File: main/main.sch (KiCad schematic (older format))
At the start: 2 parts, among them J2 AudioJack3, J3 Conn_02x10_Odd_Even

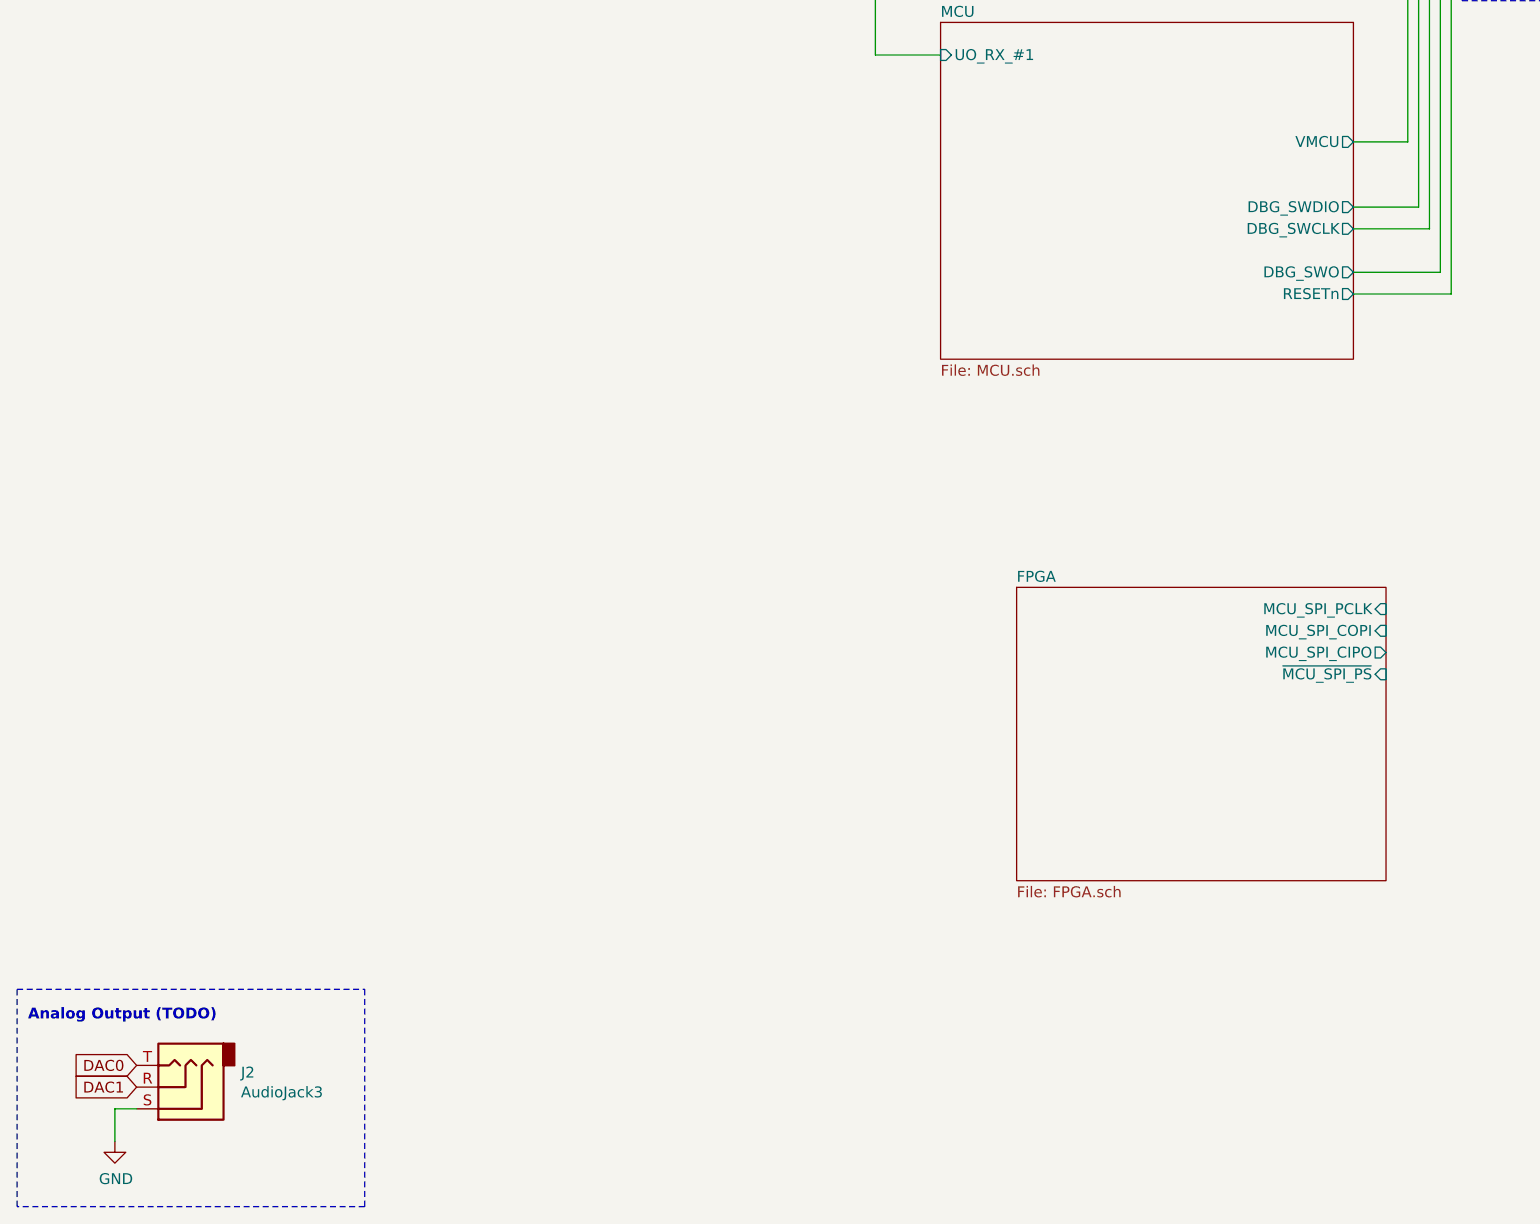
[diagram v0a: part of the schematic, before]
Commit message: Setup DAC.
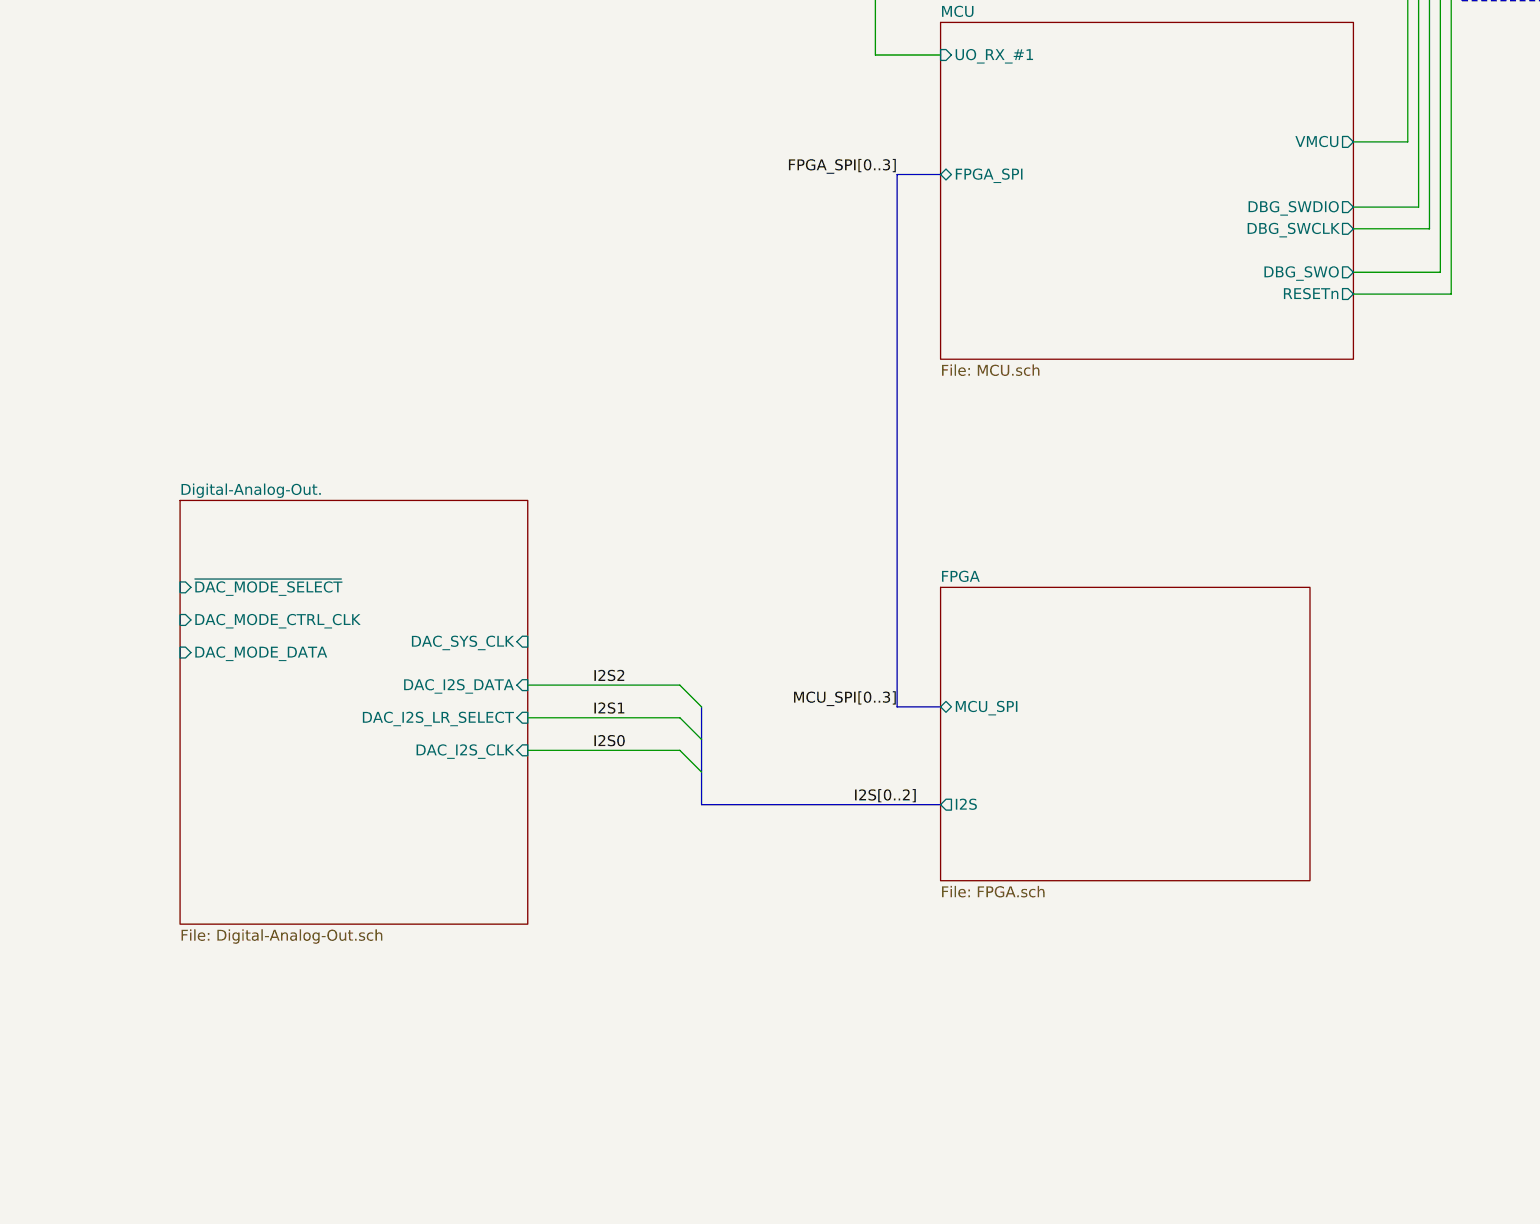
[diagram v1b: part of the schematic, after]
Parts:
- removed J2: AudioJack3, symbol Connector:AudioJack3
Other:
- note removed: "Analog Output (TODO)"
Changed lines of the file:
@@
 $Descr A4 11693 8268
 encoding utf-8
-Sheet 1 4
+Sheet 1 5
 Title "Synthesizer"
 Date "2021-09-06"
@@
 Comment4 "TDT4295 Computer Design Project"
 $EndDescr
-$Comp
-L Connector:AudioJack3 J2
-U 1 1 61366BDF
-P 1300 7150
-F 0 "J2" H 1020 7083 50  0000 R CNN
-F 1 "AudioJack3" H 1020 7174 50  0000 R CNN
-F 2 "" H 1300 7150 50  0001 C CNN
-F 3 "~" H 1300 7150 50  0001 C CNN
-	1    1300 7150
-	-1   0    0    1
-$EndComp
-$Comp
-L power:GND #PWR0101
-U 1 1 61367C82
-P 1000 7400
-F 0 "#PWR0101" H 1000 7150 50  0001 C CNN
-F 1 "GND" H 1005 7227 50  0000 C CNN
-F 2 "" H 1000 7400 50  0001 C CNN
-F 3 "" H 1000 7400 50  0001 C CNN
-	1    1000 7400
-	1    0    0    -1
-$EndComp
-Wire Wire Line
-	1000 7400 1000 7250
-Wire Wire Line
-	1000 7250 1100 7250
-Text GLabel 1100 7050 0    50   Input ~ 0
-DAC0
-Text GLabel 1100 7150 0    50   Input ~ 0
-DAC1
-Wire Notes Line
-	550  6700 2150 6700
-Wire Notes Line
-	2150 7700 550  7700
-Text Notes 600  6850 0    50   ~ 10
-Analog Output (TODO)
-Wire Notes Line
-	2150 6700 2150 7700
-Wire Notes Line
-	550  7700 550  6700
 Wire Notes Line
 	11150 550  7200 550
-$Sheet
-S 4800 2250 1900 1550
-U 6139E7E0
-F0 "MCU" 50
-F1 "MCU.sch" 50
-F2 "DBG_SWDIO" O R 6700 3100 50
-F3 "DBG_SWCLK" O R 6700 3200 50
-F4 "DBG_SWO" O R 6700 3400 50
-F5 "RESETn" O R 6700 3500 50
-F6 "VMCU" O R 6700 2800 50
-F7 "UO_RX_#1" I L 4800 2400 50
-$EndSheet
 $Sheet
 S 3450 700  700  250
@@
 	4500 2400 4800 2400
 $Sheet
-S 5150 4850 1700 1350
+S 1300 4450 1600 1950
+U 61417224
+F0 "Digital-Analog-Out." 50
+F1 "Digital-Analog-Out.sch" 50
+F2 "~DAC_MODE_SELECT" I L 1300 4850 50
+F3 "DAC_MODE_CTRL_CLK" I L 1300 5000 50
+F4 "DAC_MODE_DATA" I L 1300 5150 50
+F5 "DAC_SYS_CLK" I R 2900 5100 50
+F6 "DAC_I2S_DATA" I R 2900 5300 50
+F7 "DAC_I2S_CLK" I R 2900 5600 50
+F8 "DAC_I2S_LR_SELECT" I R 2900 5450 50
+$EndSheet
+Entry Wire Line
+	3600 5300 3700 5400
+Entry Wire Line
+	3600 5450 3700 5550
+Entry Wire Line
+	3600 5600 3700 5700
+Wire Wire Line
+	2900 5300 3600 5300
+Wire Wire Line
+	2900 5450 3600 5450
+Wire Wire Line
+	2900 5600 3600 5600
+Text Label 4400 5850 0    50   ~ 0
+I2S[0..2]
+Text Label 3200 5300 0    50   ~ 0
+I2S2
+Text Label 3200 5450 0    50   ~ 0
+I2S1
+Text Label 3200 5600 0    50   ~ 0
+I2S0
+Wire Bus Line
+	3700 5850 4800 5850
+$Sheet
+S 4800 2250 1900 1550
+U 6139E7E0
+F0 "MCU" 50
+F1 "MCU.sch" 50
+F2 "DBG_SWDIO" O R 6700 3100 50
+F3 "DBG_SWCLK" O R 6700 3200 50
+F4 "DBG_SWO" O R 6700 3400 50
+F5 "RESETn" O R 6700 3500 50
+F6 "VMCU" O R 6700 2800 50
+F7 "UO_RX_#1" I L 4800 2400 50
+F8 "FPGA_SPI" B L 4800 2950 50
+$EndSheet
+$Sheet
+S 4800 4850 1700 1350
 U 613F0EEF
 F0 "FPGA" 50
 F1 "FPGA.sch" 50
-F2 "MCU_SPI_PCLK" I R 6850 4950 50
-F3 "MCU_SPI_COPI" I R 6850 5050 50
-F4 "MCU_SPI_CIPO" O R 6850 5150 50
-F5 "~MCU_SPI_PS" I R 6850 5250 50
-$EndSheet
+F2 "I2S" O L 4800 5850 50
+F3 "MCU_SPI" B L 4800 5400 50
+$EndSheet
+Wire Bus Line
+	4800 2950 4600 2950
+Wire Bus Line
+	4600 2950 4600 5400
+Wire Bus Line
+	4600 5400 4800 5400
+Text Label 4600 5400 2    50   ~ 0
+MCU_SPI[0..3]
+Text Label 4600 2950 2    50   ~ 0
+FPGA_SPI[0..3]
+Wire Bus Line
+	3700 5400 3700 5850
 $EndSCHEMATC

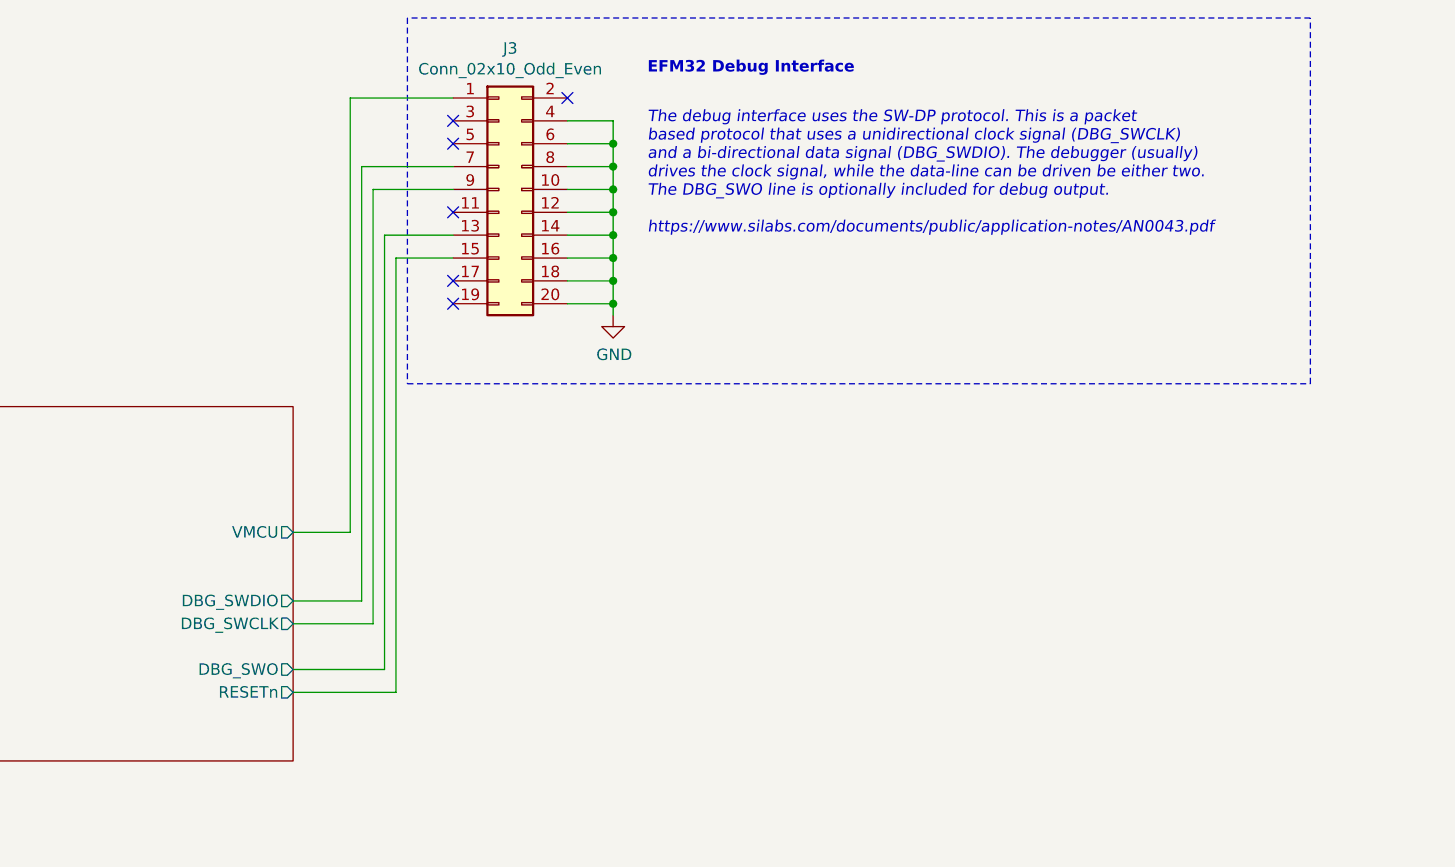
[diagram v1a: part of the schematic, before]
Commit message: Move EFM32GG debug port inside MCU sheet
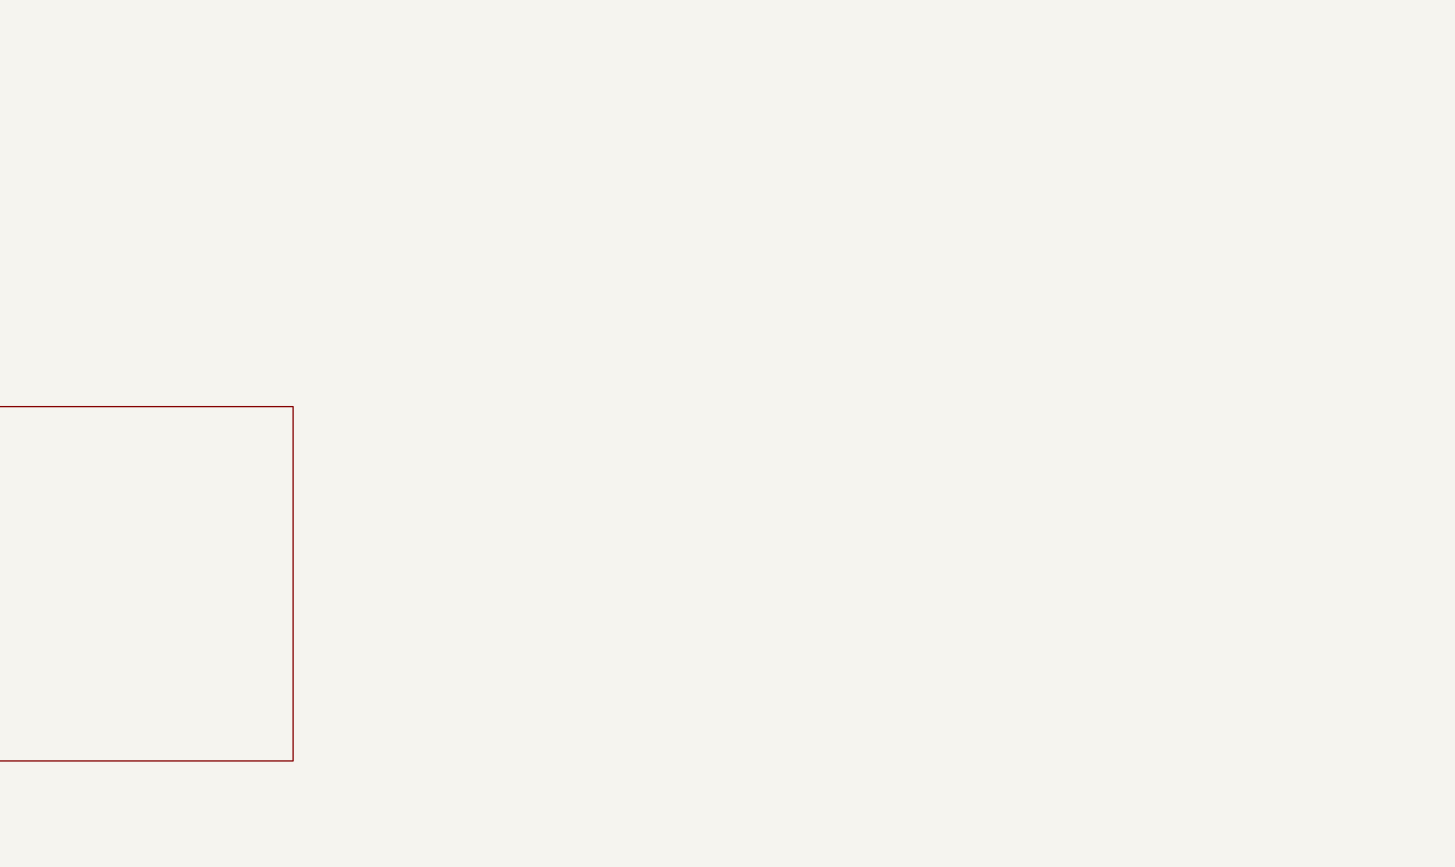
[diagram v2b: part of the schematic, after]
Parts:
- removed J3: Conn_02x10_Odd_Even, symbol Connector_Generic:Conn_02x10_Odd_Even
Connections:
- no-connect marks 6 -> 0
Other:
- note removed: "EFM32 Debug Interface"
- note removed: "The debug interface uses the SW-DP protocol. This is a packet \nbased protocol that uses a unidirectional clock signal (DBG_SWCLK) \nand a bi-directional data signal (DBG_SWDIO). The debugger (usually)\ndrives the clock signal, while the data-line can be driven be either two.\nThe DBG_SWO line is optionally included for debug output.\n\nhttps://www.silabs.com/documents/public/application-notes/AN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"
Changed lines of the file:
@@
 Comment4 "TDT4295 Computer Design Project"
 $EndDescr
-Wire Notes Line
-	11150 550  7200 550
 $Sheet
 S 3450 700  700  250
@@
 F2 "MIDI_IN" O R 4150 850 50
 $EndSheet
-Text Notes 8250 1500 0    50   Italic 0
-The debug interface uses the SW-DP protocol. This is a packet \nbased protocol that uses a unidirectional clock signal (DBG_SWCLK) \nand a bi-directional data signal (DBG_SWDIO). The debugger (usually)\ndrives the clock signal, while the data-line can be driven be either two.\nThe DBG_SWO line is optionally included for debug output.\n\nhttps://www.silabs.com/documents/public/application-notes/AN0043.pdf
-NoConn ~ 7400 1800
-NoConn ~ 7400 1700
-Wire Wire Line
-	8100 1100 8100 1200
-Connection ~ 8100 1100
-Wire Wire Line
-	8100 1000 8100 1100
-Wire Wire Line
-	7900 1000 8100 1000
-Connection ~ 8100 1200
-Wire Wire Line
-	7900 1100 8100 1100
-Wire Wire Line
-	8100 1300 8100 1400
-Connection ~ 8100 1300
-Wire Wire Line
-	8100 1200 8100 1300
-Wire Wire Line
-	7900 1200 8100 1200
-Connection ~ 8100 1400
-Wire Wire Line
-	7900 1300 8100 1300
-Wire Wire Line
-	8100 1500 8100 1600
-Connection ~ 8100 1500
-Wire Wire Line
-	8100 1400 8100 1500
-Wire Wire Line
-	7900 1400 8100 1400
-Wire Wire Line
-	8100 1600 8100 1700
-Connection ~ 8100 1600
-Wire Wire Line
-	7900 1500 8100 1500
-Connection ~ 8100 1700
-Wire Wire Line
-	7900 1600 8100 1600
-Wire Wire Line
-	8100 1800 8100 1850
-Connection ~ 8100 1800
-Wire Wire Line
-	8100 1700 8100 1800
-Wire Wire Line
-	7900 1700 8100 1700
-Wire Wire Line
-	7900 1800 8100 1800
-$Comp
-L power:GND #PWR04
-U 1 1 613B8CA5
-P 8100 1850
-F 0 "#PWR04" H 8100 1600 50  0001 C CNN
-F 1 "GND" H 8105 1677 50  0000 C CNN
-F 2 "" H 8100 1850 50  0001 C CNN
-F 3 "" H 8100 1850 50  0001 C CNN
-	1    8100 1850
-	1    0    0    -1
-$EndComp
-NoConn ~ 7400 1400
-NoConn ~ 7400 1100
-NoConn ~ 7400 1000
-NoConn ~ 7900 900
-$Comp
-L Connector_Generic:Conn_02x10_Odd_Even J3
-U 1 1 613A6A76
-P 7600 1300
-F 0 "J3" H 7650 1917 50  0000 C CNN
-F 1 "Conn_02x10_Odd_Even" H 7650 1826 50  0000 C CNN
-F 2 "" H 7600 1300 50  0001 C CNN
-F 3 "~" H 7600 1300 50  0001 C CNN
-	1    7600 1300
-	1    0    0    -1
-$EndComp
-Text Notes 8250 800  0    50   ~ 10
-EFM32 Debug Interface
-Wire Notes Line
-	7200 550  7200 2150
-Wire Notes Line
-	11150 2150 11150 550
-Wire Notes Line
-	7200 2150 11150 2150
-Wire Wire Line
-	6700 2800 6950 2800
-Wire Wire Line
-	6950 2800 6950 900
-Wire Wire Line
-	6950 900  7400 900
-Wire Wire Line
-	6700 3100 7000 3100
-Wire Wire Line
-	7000 3100 7000 1200
-Wire Wire Line
-	7000 1200 7400 1200
-Wire Wire Line
-	6700 3200 7050 3200
-Wire Wire Line
-	7050 3200 7050 1300
-Wire Wire Line
-	7050 1300 7400 1300
-Wire Wire Line
-	6700 3400 7100 3400
-Wire Wire Line
-	7100 3400 7100 1500
-Wire Wire Line
-	7100 1500 7400 1500
-Wire Wire Line
-	6700 3500 7150 3500
-Wire Wire Line
-	7150 3500 7150 1600
-Wire Wire Line
-	7150 1600 7400 1600
 Wire Wire Line
 	4150 850  4500 850
@@
 	3700 5850 4800 5850
 $Sheet
-S 4800 2250 1900 1550
-U 6139E7E0
-F0 "MCU" 50
-F1 "MCU.sch" 50
-F2 "DBG_SWDIO" O R 6700 3100 50
-F3 "DBG_SWCLK" O R 6700 3200 50
-F4 "DBG_SWO" O R 6700 3400 50
-F5 "RESETn" O R 6700 3500 50
-F6 "VMCU" O R 6700 2800 50
-F7 "UO_RX_#1" I L 4800 2400 50
-F8 "FPGA_SPI" B L 4800 2950 50
-$EndSheet
-$Sheet
 S 4800 4850 1700 1350
 U 613F0EEF
@@
 Text Label 4600 2950 2    50   ~ 0
 FPGA_SPI[0..3]
+$Sheet
+S 4800 2250 1900 1550
+U 6139E7E0
+F0 "MCU" 50
+F1 "MCU.sch" 50
+F2 "UO_RX_#1" I L 4800 2400 50
+F3 "FPGA_SPI" B L 4800 2950 50
+$EndSheet
 Wire Bus Line
 	3700 5400 3700 5850
